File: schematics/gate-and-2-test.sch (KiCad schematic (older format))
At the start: 1 part

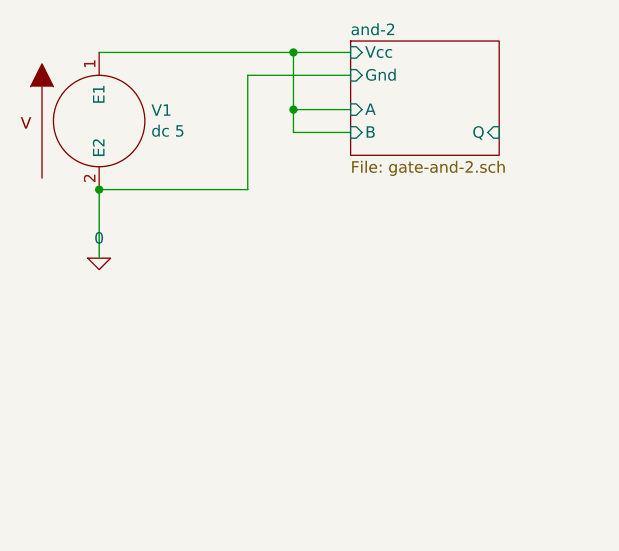
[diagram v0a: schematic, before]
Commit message: Adds some tests for and-2, nor-2, nor-3
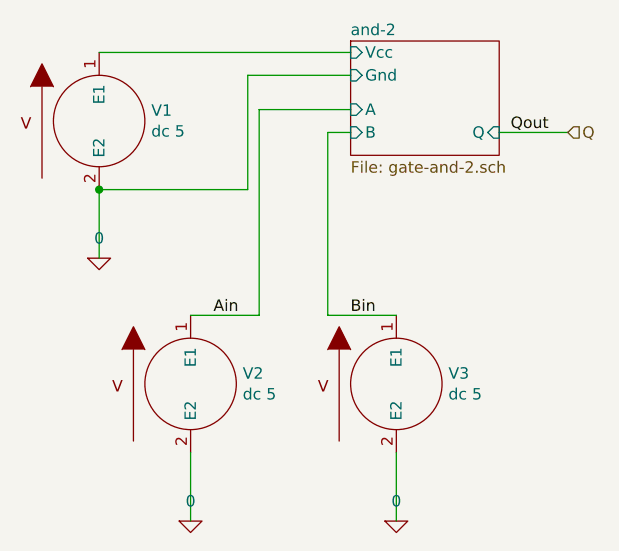
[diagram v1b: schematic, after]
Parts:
- added V2, V3: dc 5, symbol pspice:VSOURCE
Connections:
- net 0: now also V2.2 (E2), V3.2 (E2)
- net and-2/A renamed and-2/Vcc
- new net Ain: V2.1 (E1)
- new net Bin: V3.1 (E1)
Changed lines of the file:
@@
 EESchema Schematic File Version 4
+LIBS:gate-and-2-test-cache
 EELAYER 26 0
 EELAYER END
@@
 $EndComp
 $Comp
-L pspice:0 #GND0101
+L pspice:0 #GND01
 U 1 1 5C3FE2DF
 P 3550 4000
-F 0 "#GND0101" H 3550 3900 50  0001 C CNN
+F 0 "#GND01" H 3550 3900 50  0001 C CNN
 F 1 "0" H 3550 4087 50  0000 C CNN
 F 2 "" H 3550 4000 50  0001 C CNN
@@
 $EndSheet
 Wire Wire Line
-	4650 3100 4400 3100
-Wire Wire Line
 	4650 3200 4200 3200
 Wire Wire Line
@@
 Connection ~ 3550 3700
 Wire Wire Line
-	4400 3350 4650 3350
-Connection ~ 4400 3100
+	3550 3100 4650 3100
+Text HLabel 5600 3450 2    50   Input ~ 0
+Q
 Wire Wire Line
-	4400 3100 3550 3100
+	5600 3450 5300 3450
+Text Label 5350 3450 0    50   ~ 0
+Qout
+$Comp
+L pspice:VSOURCE V2
+U 1 1 5C56A30D
+P 3950 4550
+F 0 "V2" H 4178 4596 50  0000 L CNN
+F 1 "dc 5" H 4178 4505 50  0000 L CNN
+F 2 "" H 3950 4550 50  0001 C CNN
+F 3 "~" H 3950 4550 50  0001 C CNN
+	1    3950 4550
+	1    0    0    -1
+$EndComp
+$Comp
+L pspice:0 #GND02
+U 1 1 5C56A314
+P 3950 5150
+F 0 "#GND02" H 3950 5050 50  0001 C CNN
+F 1 "0" H 3950 5237 50  0000 C CNN
+F 2 "" H 3950 5150 50  0001 C CNN
+F 3 "~" H 3950 5150 50  0001 C CNN
+	1    3950 5150
+	1    0    0    -1
+$EndComp
 Wire Wire Line
-	4650 3450 4400 3450
+	3950 5150 3950 4850
+$Comp
+L pspice:VSOURCE V3
+U 1 1 5C56A384
+P 4850 4550
+F 0 "V3" H 5078 4596 50  0000 L CNN
+F 1 "dc 5" H 5078 4505 50  0000 L CNN
+F 2 "" H 4850 4550 50  0001 C CNN
+F 3 "~" H 4850 4550 50  0001 C CNN
+	1    4850 4550
+	1    0    0    -1
+$EndComp
+$Comp
+L pspice:0 #GND03
+U 1 1 5C56A38B
+P 4850 5150
+F 0 "#GND03" H 4850 5050 50  0001 C CNN
+F 1 "0" H 4850 5237 50  0000 C CNN
+F 2 "" H 4850 5150 50  0001 C CNN
+F 3 "~" H 4850 5150 50  0001 C CNN
+	1    4850 5150
+	1    0    0    -1
+$EndComp
 Wire Wire Line
-	4400 3100 4400 3350
-Connection ~ 4400 3350
+	4850 5150 4850 4850
 Wire Wire Line
-	4400 3350 4400 3450
+	4650 3350 4250 3350
+Wire Wire Line
+	4250 3350 4250 4250
+Wire Wire Line
+	4250 4250 3950 4250
+Wire Wire Line
+	4650 3450 4550 3450
+Wire Wire Line
+	4550 3450 4550 4250
+Wire Wire Line
+	4550 4250 4850 4250
+Text Label 4050 4250 0    50   ~ 0
+Ain
+Text Label 4650 4250 0    50   ~ 0
+Bin
 $EndSCHEMATC
